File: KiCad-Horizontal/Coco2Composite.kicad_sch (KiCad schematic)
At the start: 19 parts, among them J1 MA03-1, J2 MA05-1, J3 AUDIO_JACK_3.5MM_PTH, Q1 PN2907, Q2 2N2222, U1 MC1372

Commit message: Increased the footprint for the resistors since the one I picked was still too small
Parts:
- R1, R4, R5, R6, R7: footprint Resistor_THT:R_Axial_DIN0204_L3.6mm_D1.6mm_P5.08mm_Horizontal -> Resistor_THT:R_Axial_DIN0207_L6.3mm_D2.5mm_P7.62mm_Horizontal
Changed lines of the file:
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@@
 			)
 		)
-		(property "Footprint" "Resistor_THT:R_Axial_DIN0204_L3.6mm_D1.6mm_P5.08mm_Horizontal"
+		(property "Footprint" "Resistor_THT:R_Axial_DIN0207_L6.3mm_D2.5mm_P7.62mm_Horizontal"
 			(at 220.98 114.3 0)
 			(effects
@@
 			)
 		)
-		(property "Footprint" "Resistor_THT:R_Axial_DIN0204_L3.6mm_D1.6mm_P5.08mm_Horizontal"
+		(property "Footprint" "Resistor_THT:R_Axial_DIN0207_L6.3mm_D2.5mm_P7.62mm_Horizontal"
 			(at 185.42 114.3 0)
 			(effects
@@
 			)
 		)
-		(property "Footprint" "Resistor_THT:R_Axial_DIN0204_L3.6mm_D1.6mm_P5.08mm_Horizontal"
+		(property "Footprint" "Resistor_THT:R_Axial_DIN0207_L6.3mm_D2.5mm_P7.62mm_Horizontal"
 			(at 134.62 58.42 0)
 			(effects
@@
 			)
 		)
-		(property "Footprint" "Resistor_THT:R_Axial_DIN0204_L3.6mm_D1.6mm_P5.08mm_Horizontal"
+		(property "Footprint" "Resistor_THT:R_Axial_DIN0207_L6.3mm_D2.5mm_P7.62mm_Horizontal"
 			(at 200.66 121.92 0)
 			(effects
@@
 			)
 		)
-		(property "Footprint" "Resistor_THT:R_Axial_DIN0204_L3.6mm_D1.6mm_P5.08mm_Horizontal"
+		(property "Footprint" "Resistor_THT:R_Axial_DIN0207_L6.3mm_D2.5mm_P7.62mm_Horizontal"
 			(at 238.76 121.92 0)
 			(effects

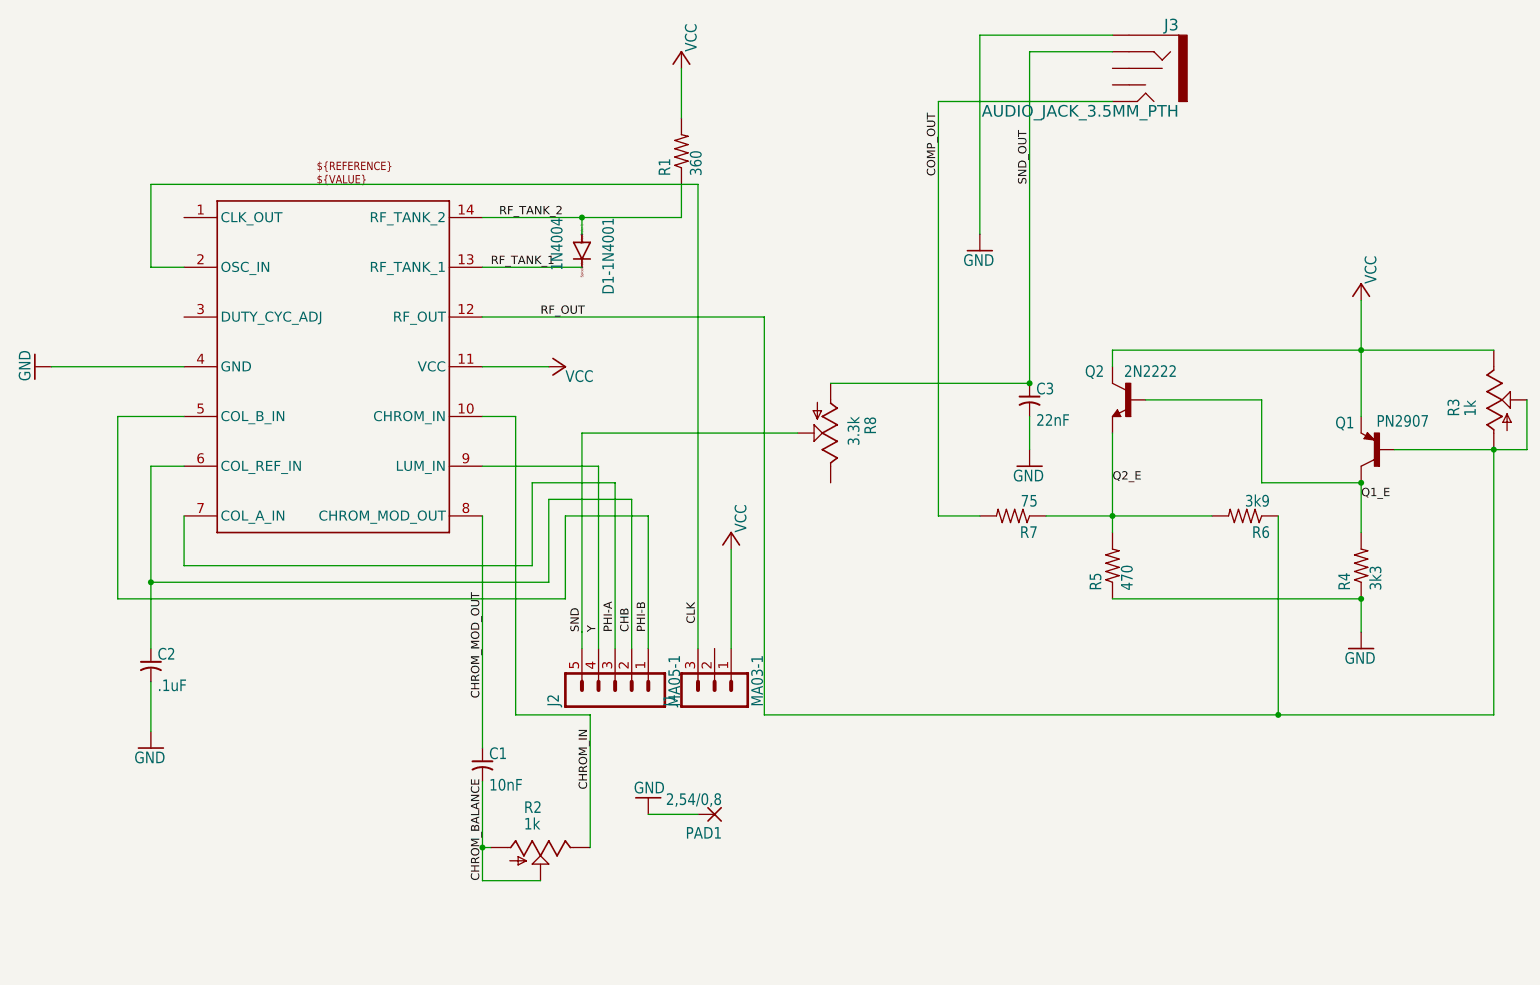
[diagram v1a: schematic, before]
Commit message: Big changes to let the channel select switch disable color
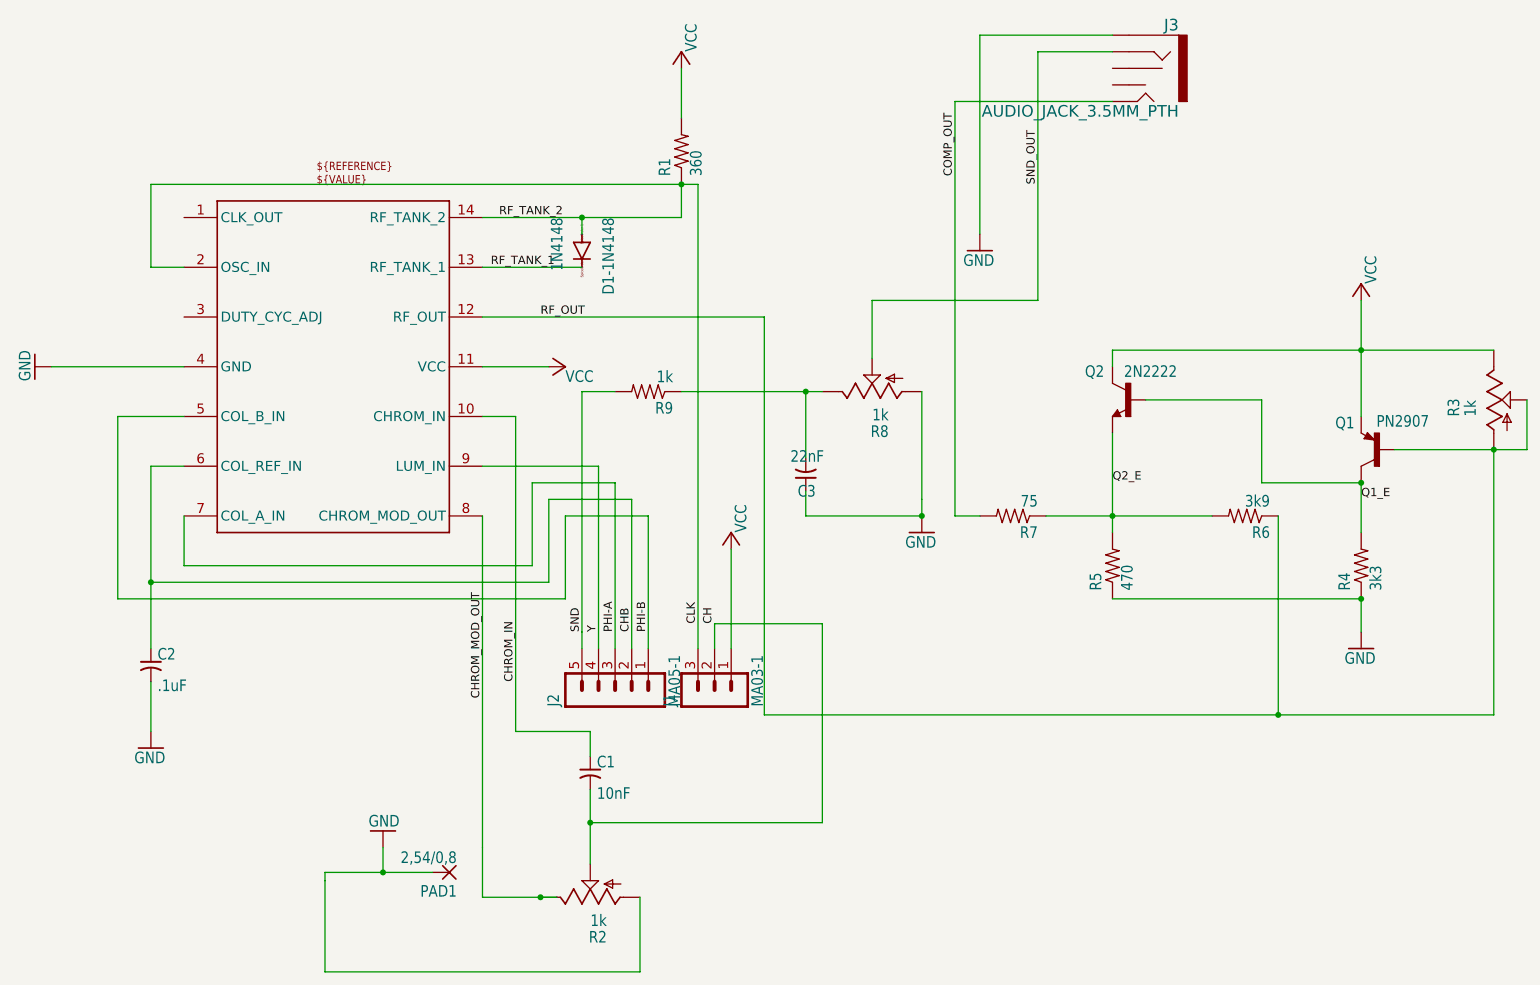
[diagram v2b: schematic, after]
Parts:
- added R9: 1k, Resistor_THT:R_Axial_DIN0207_L6.3mm_D2.5mm_P7.62mm_Horizontal, symbol Coco2Composite-eagle-import:R-US_0204/2V
- D1-1N4148: renamed from D1-1N4001; value 1N4004 -> 1N4148
- R8: value 3.3k -> 1k
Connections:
- net RF_TANK_2 is gone; now on net CLK: D1-1N4148.A, R1.1, U1.14 (RF_TANK_2)
- net CHROM_IN: now also C1.1; no longer R2.E
- net CHROM_MOD_OUT: now also R2.E; no longer C1.1
- net GND: now also C3.1, R2.A, R8.A; no longer C3.2
- net SND: now also R9.2; no longer R8.S
- net SND_OUT: now also R8.S; no longer C3.1, R8.A
- net at R8.E: now also C3.2, R9.1
- net CH: now reaches J1.2
- net CH: now also C1.2, R2.S
- removed net CHROM_BALANCE: C1.2, R2.A, R2.S
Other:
- moved on the sheet: C1, C3, PAD1, R2, R8

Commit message: increased the footprint of the variable resistors to match what I have in the BOM, added a dot for orientation, switched schematic symbols to something more standard
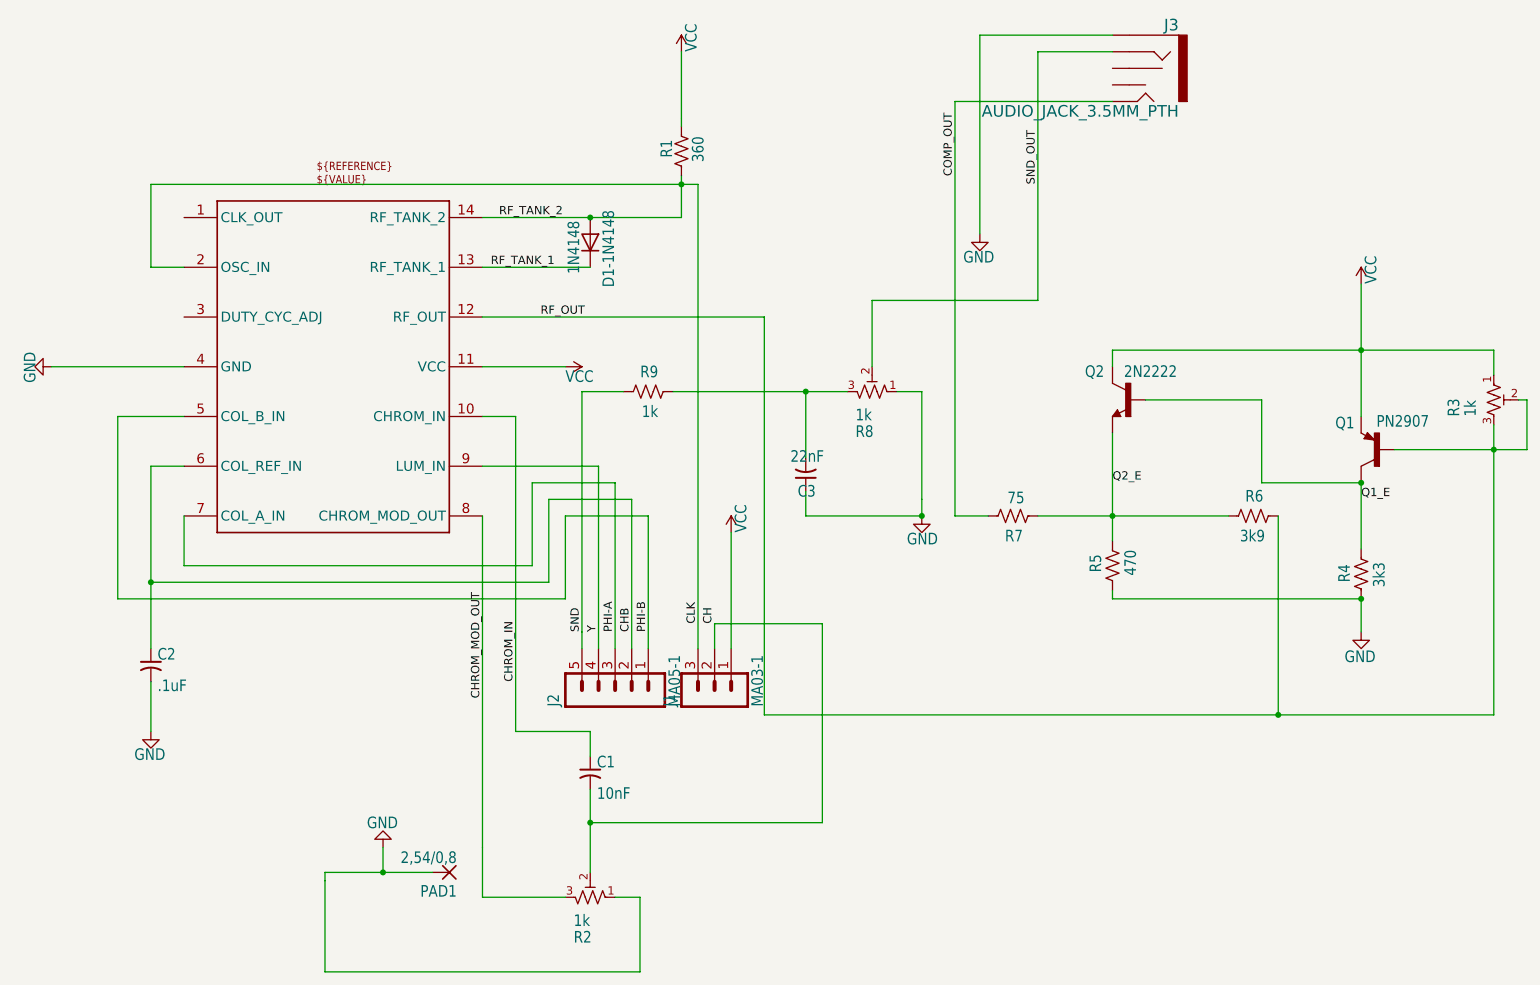
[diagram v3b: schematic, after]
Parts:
- D1-1N4148: footprint Diode_THT:D_T-1_P10.16mm_Horizontal -> Diode_THT:D_DO-35_SOD27_P7.62mm_Horizontal; symbol Coco2Composite-eagle-import:1N4004 -> Diode:1N4148
- R1, R4, R5, R6, R7, R9: symbol Coco2Composite-eagle-import:R-US_0204/2V -> Device:R_US
- R2, R3, R8: symbol Coco2Composite-eagle-import:TRIM_US-B25U -> Device:R_Potentiometer_Trim_US
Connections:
- net CH: now also R2.2; no longer R2.S
- net CHROM_MOD_OUT: now also R2.3; no longer R2.E
- net CLK: now also D1-1N4148.2 (A); no longer D1-1N4148.A
- net COMP_OUT: now also R7.1; no longer R7.2
- net GND: now also R2.1, R4.2, R5.2, R8.1; no longer R2.A, R4.1, R5.1, R8.A
- net Q1_E: now also R4.1; no longer R4.2
- net Q2_E: now also R5.1, R6.1, R7.2; no longer R5.2, R6.2, R7.1
- net RF_OUT: now also R3.2, R3.3, R6.2; no longer R3.A, R3.S, R6.1
- net RF_TANK_1: now also D1-1N4148.1 (K); no longer D1-1N4148.C
- net SND: now also R9.1; no longer R9.2
- net SND_OUT: now also R8.2; no longer R8.S
- net VCC: now also R3.1; no longer R3.E
- new net: C3.2, R8.3, R9.2

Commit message: Changed diode footprint for smaller diode
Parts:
- D1-1N4148: footprint Diode_THT:D_DO-35_SOD27_P7.62mm_Horizontal -> Diode_THT:D_DO-35_SOD27_P10.16mm_Horizontal
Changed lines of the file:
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@@
 			)
 		)
-		(property "Footprint" "Diode_THT:D_DO-35_SOD27_P7.62mm_Horizontal"
+		(property "Footprint" "Diode_THT:D_DO-35_SOD27_P10.16mm_Horizontal"
 			(at 120.65 72.39 0)
 			(effects

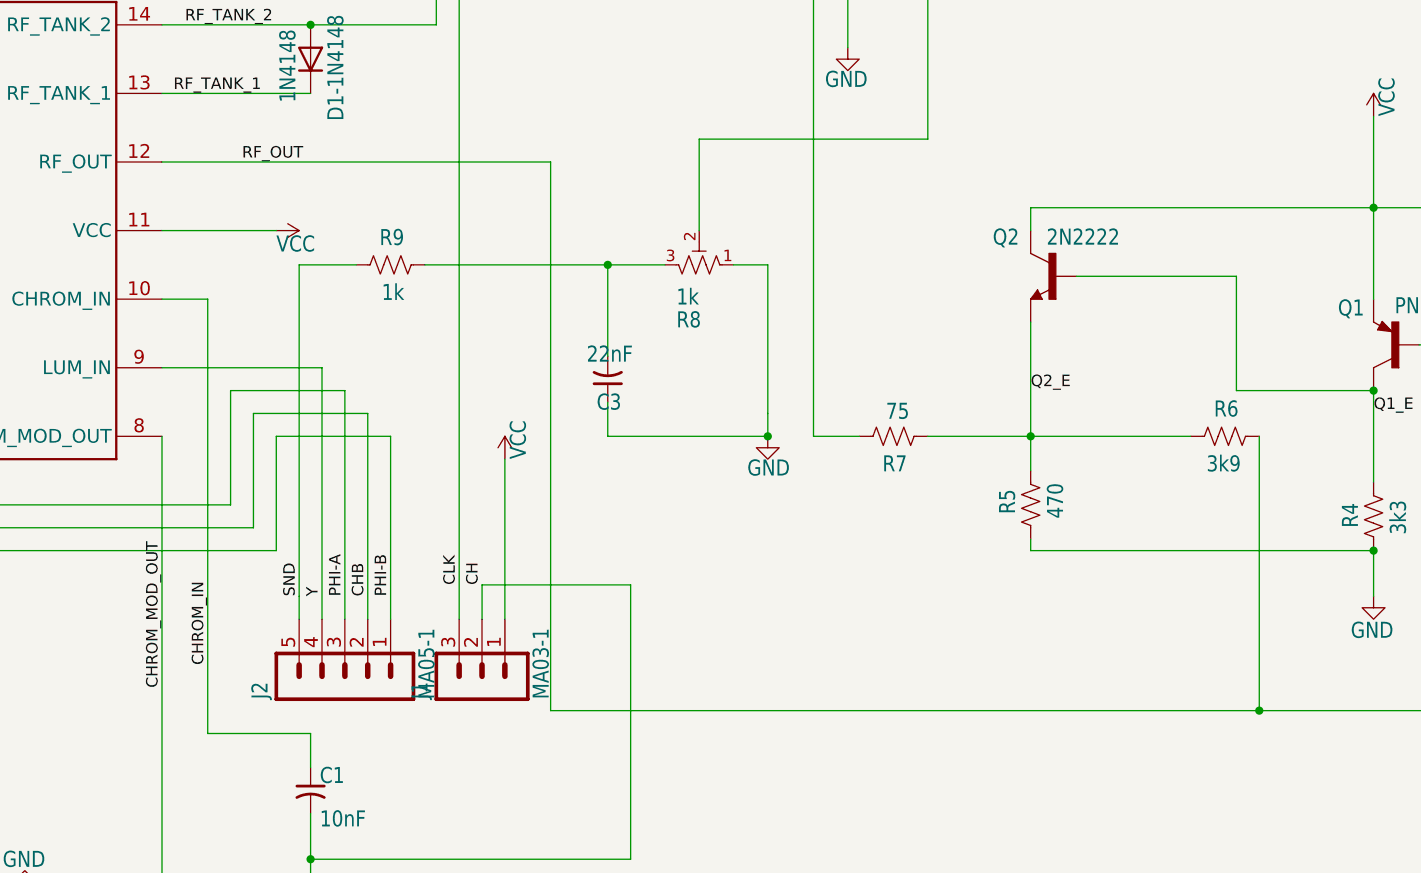
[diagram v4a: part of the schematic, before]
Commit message: Added a supply bypass capacitor
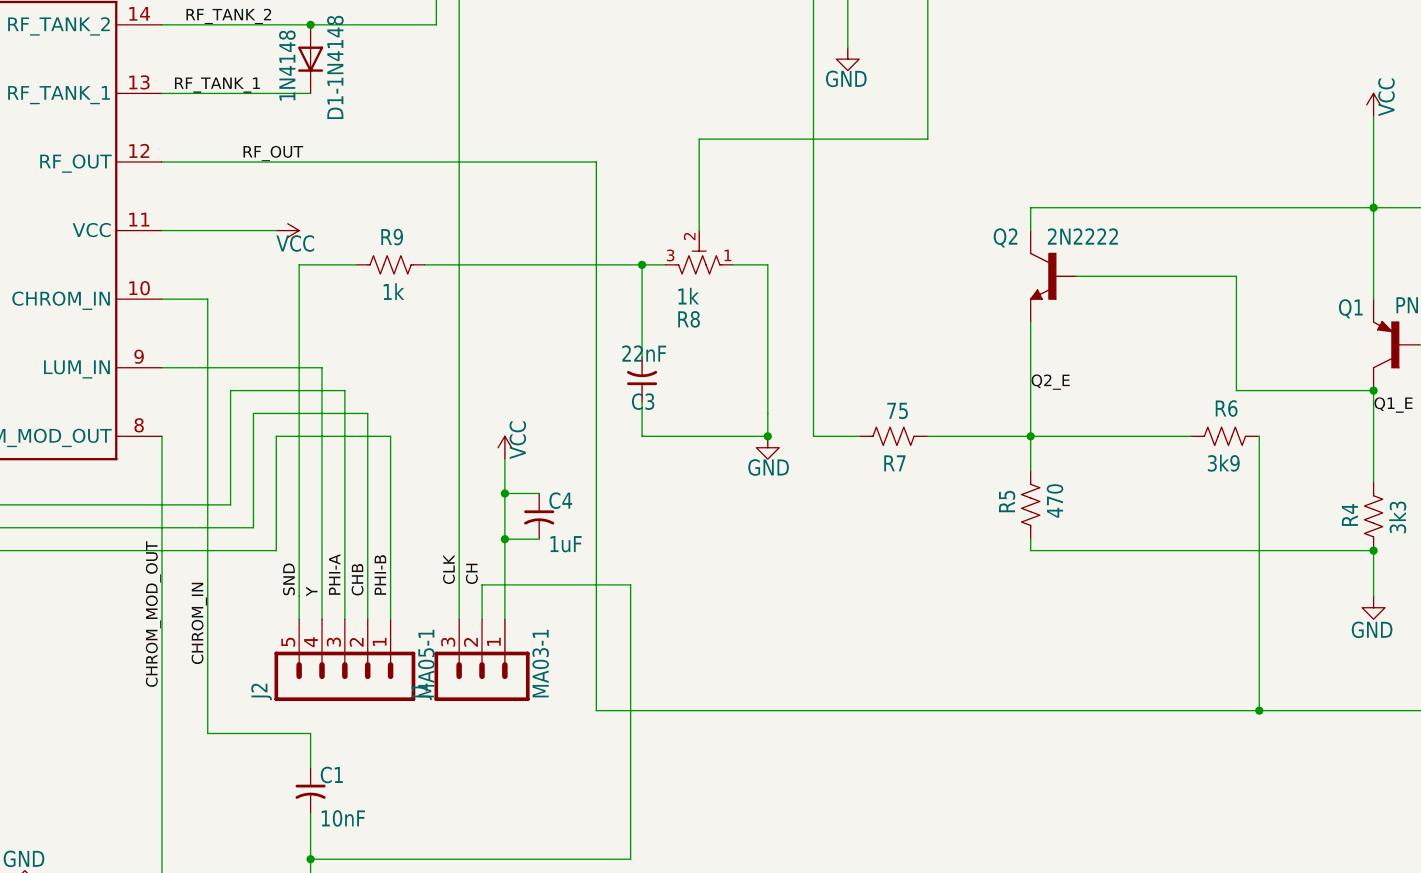
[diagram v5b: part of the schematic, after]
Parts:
- added C4: 1uF, Capacitor_THT:C_Disc_D3.0mm_W1.6mm_P2.50mm, symbol Device:C_Small_US
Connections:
- net VCC: now also C4.1, C4.2
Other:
- moved on the sheet: C3
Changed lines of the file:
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@@
-	)
-	(junction
-		(at 153.67 95.25)
-		(diameter 0)
-		(color 0 0 0 0)
 	)
 	(junction
@@
 	)
 	(junction
+		(at 142.24 125.73)
+		(diameter 0)
+		(color 0 0 0 0)
+	)
+	(junction
 		(at 53.34 124.46)
 		(diameter 0)
@@
 	)
 	(junction
+		(at 157.48 95.25)
+		(diameter 0)
+		(color 0 0 0 0)
+	)
+	(junction
 		(at 238.76 109.22)
+		(diameter 0)
+		(color 0 0 0 0)
+	)
+	(junction
+		(at 142.24 120.65)
 		(diameter 0)
 		(color 0 0 0 0)
@@
 	(wire
 		(pts
-			(xy 153.67 110.49) (xy 153.67 114.3)
+			(xy 157.48 110.49) (xy 157.48 114.3)
 		)
 		(stroke
@@
 	(wire
 		(pts
-			(xy 153.67 95.25) (xy 153.67 105.41)
+			(xy 157.48 95.25) (xy 157.48 105.41)
 		)
 		(stroke
@@
 	(wire
 		(pts
-			(xy 104.14 83.82) (xy 147.32 83.82)
+			(xy 104.14 83.82) (xy 152.4 83.82)
 		)
 		(stroke
@@
 	(wire
 		(pts
+			(xy 142.24 120.65) (xy 142.24 125.73)
+		)
+		(stroke
+			(width 0.1524)
+			(type solid)
+		)
+	)
+	(wire
+		(pts
 			(xy 80.01 168.91) (xy 88.9 168.91)
 		)
@@
 	(wire
 		(pts
-			(xy 226.06 144.78) (xy 147.32 144.78)
+			(xy 226.06 144.78) (xy 152.4 144.78)
 		)
 		(stroke
@@
 	(wire
 		(pts
-			(xy 142.24 116.84) (xy 142.24 134.62)
+			(xy 142.24 116.84) (xy 142.24 120.65)
 		)
 		(stroke
@@
 	(wire
 		(pts
-			(xy 147.32 144.78) (xy 147.32 83.82)
+			(xy 152.4 144.78) (xy 152.4 83.82)
 		)
 		(stroke
@@
 	(wire
 		(pts
+			(xy 142.24 125.73) (xy 142.24 134.62)
+		)
+		(stroke
+			(width 0.1524)
+			(type solid)
+		)
+	)
+	(wire
+		(pts
 			(xy 223.52 96.52) (xy 205.74 96.52)
 		)
@@
 	(wire
 		(pts
-			(xy 153.67 95.25) (xy 160.02 95.25)
-		)
-		(stroke
-			(width 0)
-			(type default)
-		)
-	)
-	(wire
-		(pts
 			(xy 134.62 68.58) (xy 134.62 63.5)
 		)
@@
 	(wire
 		(pts
+			(xy 157.48 95.25) (xy 160.02 95.25)
+		)
+		(stroke
+			(width 0)
+			(type default)
+		)
+	)
+	(wire
+		(pts
+			(xy 142.24 125.73) (xy 146.05 125.73)
+		)
+		(stroke
+			(width 0)
+			(type default)
+		)
+	)
+	(wire
+		(pts
 			(xy 238.76 109.22) (xy 238.76 119.38)
 		)
@@
 	(wire
 		(pts
-			(xy 133.35 95.25) (xy 153.67 95.25)
+			(xy 133.35 95.25) (xy 157.48 95.25)
 		)
 		(stroke
@@
 	(wire
 		(pts
-			(xy 153.67 114.3) (xy 171.45 114.3)
+			(xy 157.48 114.3) (xy 171.45 114.3)
 		)
 		(stroke
@@
 			(width 0.1524)
 			(type solid)
+		)
+	)
+	(wire
+		(pts
+			(xy 142.24 120.65) (xy 146.05 120.65)
+		)
+		(stroke
+			(width 0)
+			(type default)
 		)
 	)
@@
 			)
 			(justify left bottom)
+		)
+	)
+	(symbol
+		(lib_id "Device:C_Small_US")
+		(at 146.05 123.19 0)
+		(unit 1)
+		(exclude_from_sim no)
+		(in_bom yes)
+		(on_board yes)
+		(dnp no)
+		(property "Reference" "C4"
+			(at 147.066 122.555 0)
+			(effects
+				(font
+					(size 1.778 1.5113)
+				)
+				(justify left bottom)
+			)
+		)
+		(property "Value" "1uF"
+			(at 147.066 127.381 0)
+			(effects
+				(font
+					(size 1.778 1.5113)
+				)
+				(justify left bottom)
+			)
+		)
+		(property "Footprint" "Capacitor_THT:C_Disc_D3.0mm_W1.6mm_P2.50mm"
+			(at 146.05 123.19 0)
+			(effects
+				(font
+					(size 1.27 1.27)
+				)
+				(hide yes)
+			)
+		)
+		(property "Datasheet" ""
+			(at 146.05 123.19 0)
+			(effects
+				(font
+					(size 1.27 1.27)
+				)
+				(hide yes)
+			)
+		)
+		(property "Description" "capacitor, small US symbol"
+			(at 146.05 123.19 0)
+			(effects
+				(font
+					(size 1.27 1.27)
+				)
+				(hide yes)
+			)
+		)
+		(pin "1"
+		)
+		(pin "2"
+		)
+		(instances
+			(project "Coco2Composite"
+				(path "/10b578e1-d913-42e6-b9e5-398116858bd9"
+					(reference "C4")
+					(unit 1)
+				)
+			)
 		)
 	)
@@
 	(symbol
 		(lib_id "Device:C_Small_US")
-		(at 153.67 107.95 180)
+		(at 157.48 107.95 180)
 		(unit 1)
 		(exclude_from_sim no)
@@
 		(dnp no)
 		(property "Reference" "C3"
-			(at 155.194 109.474 0)
+			(at 159.004 109.474 0)
 			(effects
 				(font
@@
 		)
 		(property "Value" "22nF"
-			(at 156.464 104.14 0)
+			(at 160.274 104.14 0)
 			(effects
 				(font
@@
 		)
 		(property "Footprint" "Capacitor_THT:C_Disc_D3.0mm_W1.6mm_P2.50mm"
-			(at 153.67 107.95 0)
+			(at 157.48 107.95 0)
 			(effects
 				(font
@@
 		)
 		(property "Datasheet" ""
-			(at 153.67 107.95 0)
+			(at 157.48 107.95 0)
 			(effects
 				(font
@@
 		)
 		(property "Description" "capacitor, small US symbol"
-			(at 153.67 107.95 0)
-			(effects
-				(font
+			(at 157.48 107.95 0)
+			(effects
+				(font
